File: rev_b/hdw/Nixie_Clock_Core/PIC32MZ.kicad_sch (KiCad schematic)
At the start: 3 parts

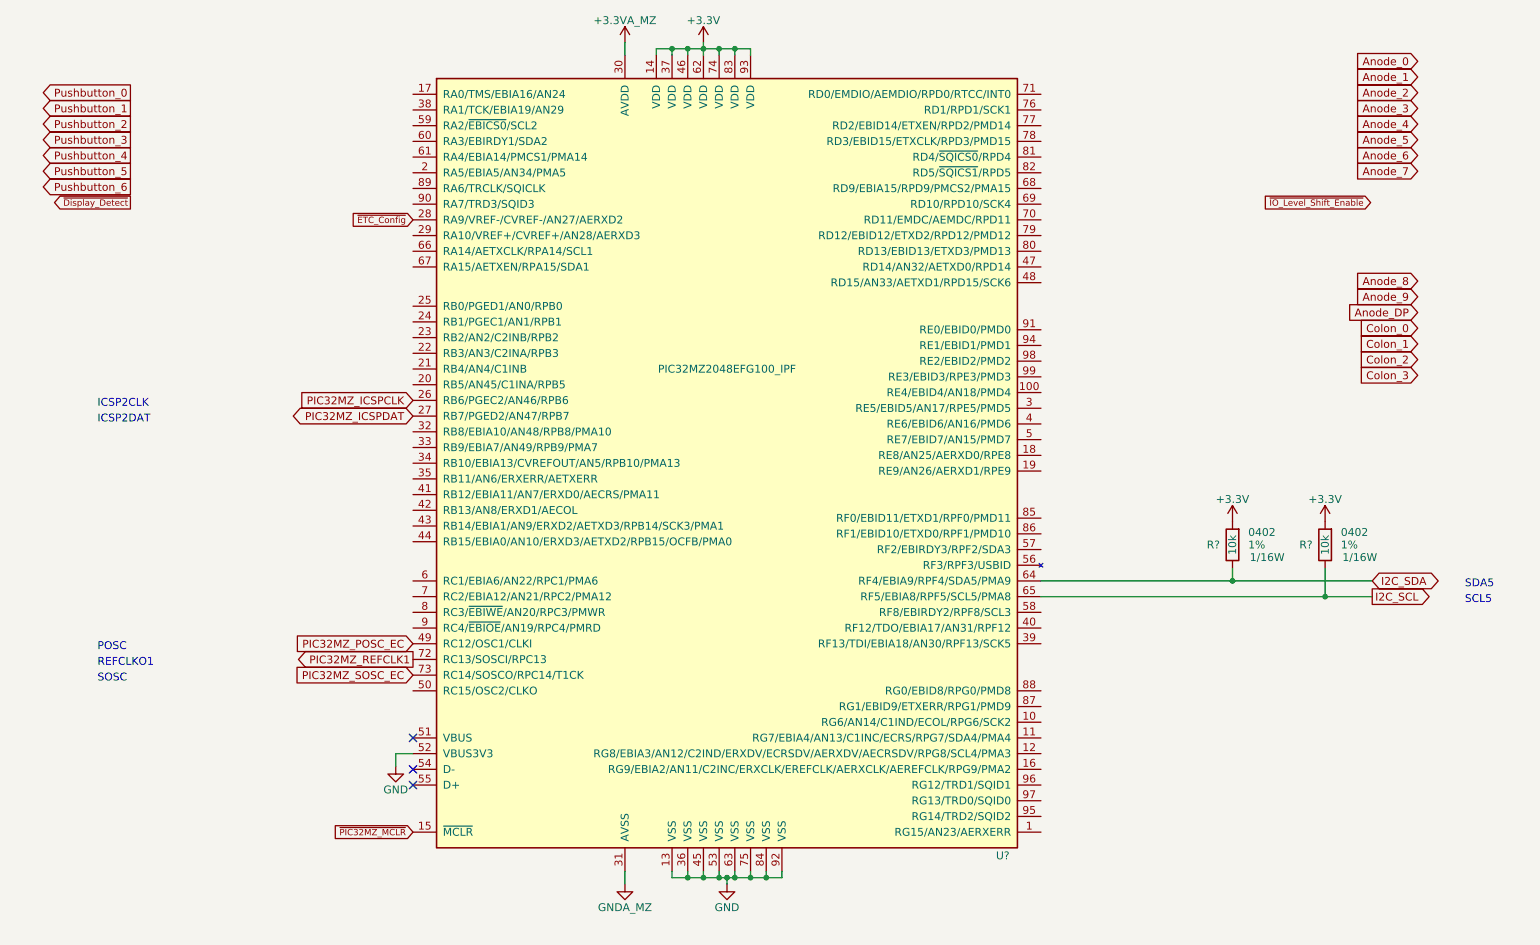
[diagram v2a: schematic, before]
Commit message: more schematic progress, assigning signals to MCU"
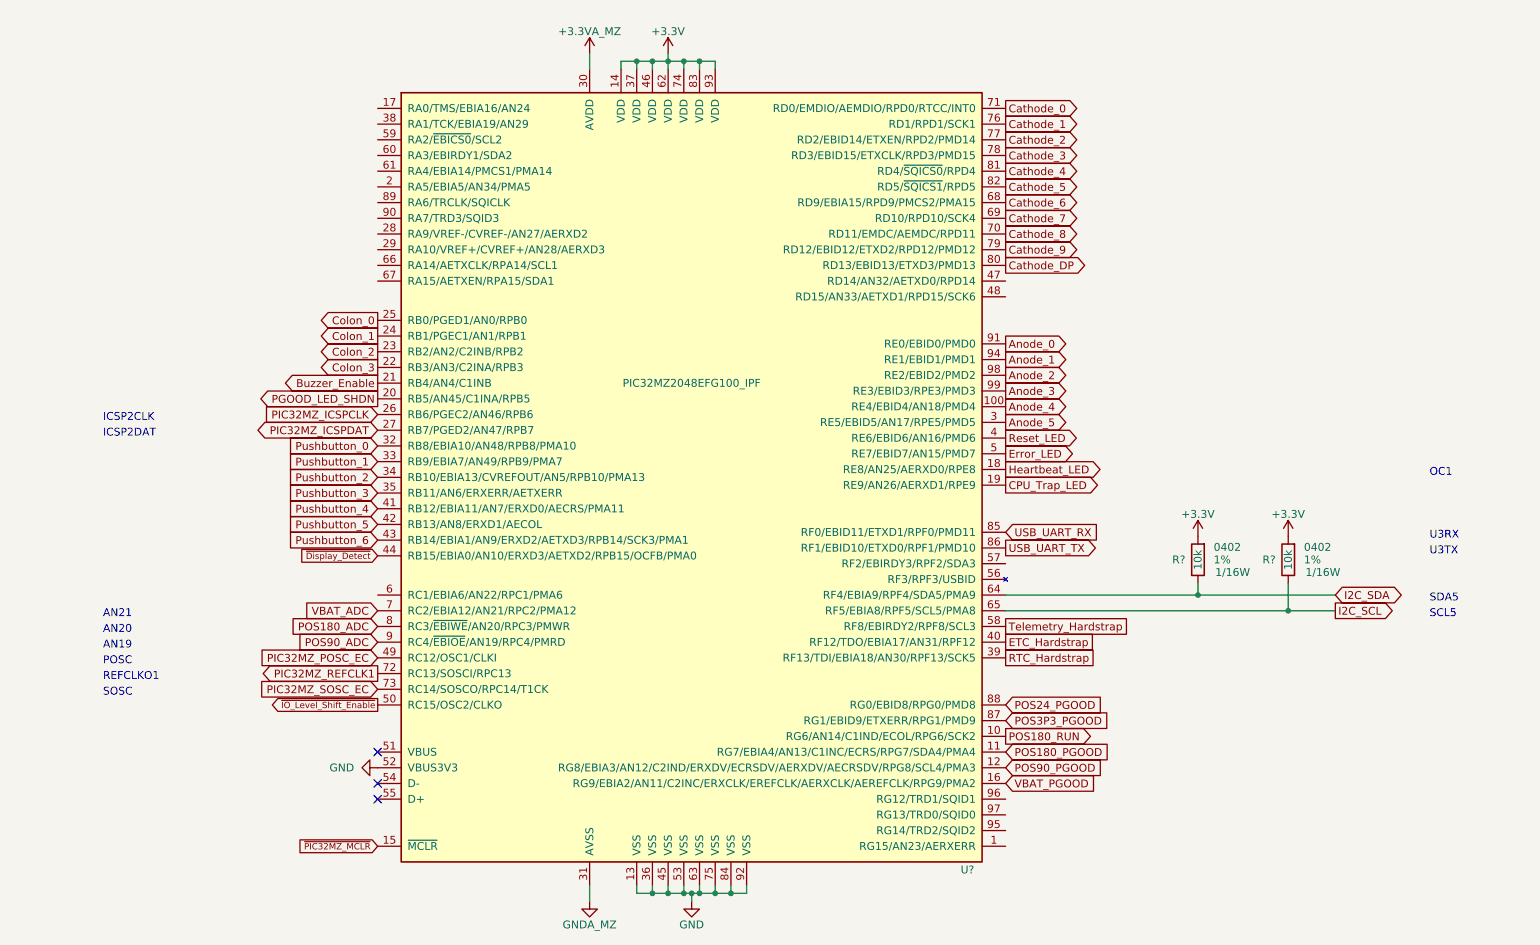
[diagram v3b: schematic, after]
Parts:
- removed U?: PIC32MZ2048EFG100_IPF, Housings_QFP:TQFP-100_14x14mm_Pitch0.5mm, symbol Custom_Library:PIC32MZ2048EFG100_IPF
- added U?: PIC32MZ2048EFG100_IPF, Housings_QFP:TQFP-100_14x14mm_Pitch0.5mm, symbol Custom Library:PIC32MZ2048EFG100_IPF
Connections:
- net +3.3V: now also U?.14 (VDD), U?.37 (VDD), U?.46 (VDD), U?.62 (VDD), U?.74 (VDD), U?.83 (VDD), U?.93 (VDD)
- net +3.3VA_MZ: now also U?.30 (AVDD)
- net Anode_0: now also U?.91 (RE0/EBID0/PMD0)
- net Anode_1: now also U?.94 (RE1/EBID1/PMD1)
- net Anode_2: now also U?.98 (RE2/EBID2/PMD2)
- net Anode_3: now also U?.99 (RE3/EBID3/RPE3/PMD3)
- net Anode_4: now also U?.100 (RE4/EBID4/AN18/PMD4)
- net Anode_5: now also U?.3 (RE5/EBID5/AN17/RPE5/PMD5)
- net Colon_0: now also U?.25 (RB0/PGED1/AN0/RPB0)
- net Colon_1: now also U?.24 (RB1/PGEC1/AN1/RPB1)
- net Colon_2: now also U?.23 (RB2/AN2/C2INB/RPB2)
- net Colon_3: now also U?.22 (RB3/AN3/C2INA/RPB3)
- net GND: now also U?.13 (VSS), U?.36 (VSS), U?.45 (VSS), U?.52 (VBUS3V3), U?.53 (VSS), U?.63 (VSS), U?.75 (VSS), U?.84 (VSS), U?.92 (VSS)
- net GNDA_MZ: now also U?.31 (AVSS)
- net I2C_SCL: now also U?.65 (RF5/EBIA8/RPF5/SCL5/PMA8)
- net I2C_SDA: now also U?.64 (RF4/EBIA9/RPF4/SDA5/PMA9)
- net PIC32MZ_ICSPCLK: now also U?.26 (RB6/PGEC2/AN46/RPB6)
- net PIC32MZ_ICSPDAT: now also U?.27 (RB7/PGED2/AN47/RPB7)
- net PIC32MZ_POSC_EC: now also U?.49 (RC12/OSC1/CLKI)
- net PIC32MZ_REFCLK1: now also U?.72 (RC13/SOSCI/RPC13)
- net PIC32MZ_SOSC_EC: now also U?.73 (RC14/SOSCO/RPC14/T1CK)
- net Pushbutton_0: now also U?.32 (RB8/EBIA10/AN48/RPB8/PMA10)
- net Pushbutton_1: now also U?.33 (RB9/EBIA7/AN49/RPB9/PMA7)
- net Pushbutton_2: now also U?.34 (RB10/EBIA13/CVREFOUT/AN5/RPB10/PMA13)
- net Pushbutton_3: now also U?.35 (RB11/AN6/ERXERR/AETXERR)
- net Pushbutton_4: now also U?.41 (RB12/EBIA11/AN7/ERXD0/AECRS/PMA11)
- net Pushbutton_5: now also U?.42 (RB13/AN8/ERXD1/AECOL)
- net Pushbutton_6: now also U?.43 (RB14/EBIA1/AN9/ERXD2/AETXD3/RPB14/SCK3/PMA1)
- net ~{Display_Detect}: now also U?.44 (RB15/EBIA0/AN10/ERXD3/AETXD2/RPB15/OCFB/PMA0)
- net ~{IO_Level_Shift_Enable}: now also U?.50 (RC15/OSC2/CLKO)
- net ~{PIC32MZ_MCLR}: now also U?.15 (~{MCLR})
- new net Buzzer_Enable: U?.21 (RB4/AN4/C1INB)
- new net CPU_Trap_LED: U?.19 (RE9/AN26/AERXD1/RPE9)
- new net Cathode_0: U?.71 (RD0/EMDIO/AEMDIO/RPD0/RTCC/INT0)
- new net Cathode_1: U?.76 (RD1/RPD1/SCK1)
- new net Cathode_2: U?.77 (RD2/EBID14/ETXEN/RPD2/PMD14)
- new net Cathode_3: U?.78 (RD3/EBID15/ETXCLK/RPD3/PMD15)
- new net Cathode_4: U?.81 (RD4/~{SQICS0}/RPD4)
- new net Cathode_5: U?.82 (RD5/~{SQICS1}/RPD5)
- new net Cathode_6: U?.68 (RD9/EBIA15/RPD9/PMCS2/PMA15)
- new net Cathode_7: U?.69 (RD10/RPD10/SCK4)
- new net Cathode_8: U?.70 (RD11/EMDC/AEMDC/RPD11)
- new net Cathode_9: U?.79 (RD12/EBID12/ETXD2/RPD12/PMD12)
- new net Cathode_DP: U?.80 (RD13/EBID13/ETXD3/PMD13)
- new net ETC_Hardstrap: U?.40 (RF12/TDO/EBIA17/AN31/RPF12)
- new net Error_LED: U?.5 (RE7/EBID7/AN15/PMD7)
- new net Heartbeat_LED: U?.18 (RE8/AN25/AERXD0/RPE8)
- new net PGOOD_LED_SHDN: U?.20 (RB5/AN45/C1INA/RPB5)
- new net POS180_ADC: U?.8 (RC3/~{EBIWE}/AN20/RPC3/PMWR)
- new net POS180_PGOOD: U?.11 (RG7/EBIA4/AN13/C1INC/ECRS/RPG7/SDA4/PMA4)
- new net POS180_RUN: U?.10 (RG6/AN14/C1IND/ECOL/RPG6/SCK2)
- new net POS24_PGOOD: U?.88 (RG0/EBID8/RPG0/PMD8)
- new net POS3P3_PGOOD: U?.87 (RG1/EBID9/ETXERR/RPG1/PMD9)
- new net POS90_ADC: U?.9 (RC4/~{EBIOE}/AN19/RPC4/PMRD)
- new net POS90_PGOOD: U?.12 (RG8/EBIA3/AN12/C2IND/ERXDV/ECRSDV/AERXDV/AECRSDV/RPG8/SCL4/PMA3)
- new net RTC_Hardstrap: U?.39 (RF13/TDI/EBIA18/AN30/RPF13/SCK5)
- new net Reset_LED: U?.4 (RE6/EBID6/AN16/PMD6)
- new net Telemetry_Hardstrap: U?.58 (RF8/EBIRDY2/RPF8/SCL3)
- new net USB_UART_RX: U?.85 (RF0/EBID11/ETXD1/RPF0/PMD11)
- new net USB_UART_TX: U?.86 (RF1/EBID10/ETXD0/RPF1/PMD10)
- new net VBAT_ADC: U?.7 (RC2/EBIA12/AN21/RPC2/PMA12)
- new net VBAT_PGOOD: U?.16 (RG9/EBIA2/AN11/C2INC/ERXCLK/EREFCLK/AERXCLK/AEREFCLK/RPG9/PMA2)
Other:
- note added: "AN19"
- note added: "AN20"
- note added: "AN21"
- note added: "OC1"
- note added: "U3RX"
- note added: "U3TX"
- moved on the sheet: R?

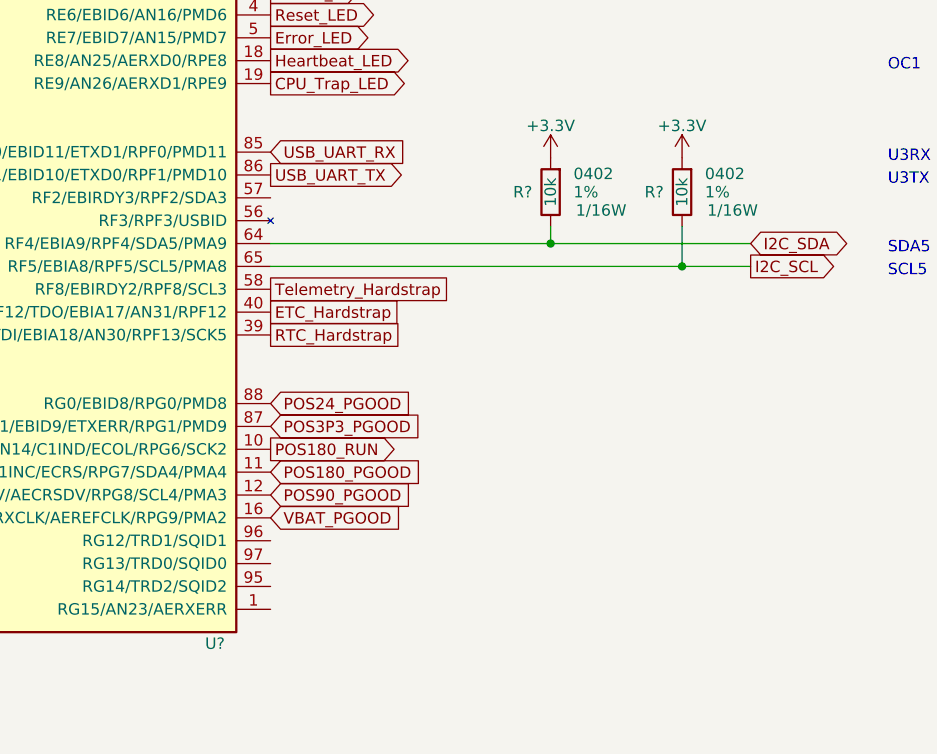
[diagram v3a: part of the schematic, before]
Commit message: updated footprints, ran some DRC
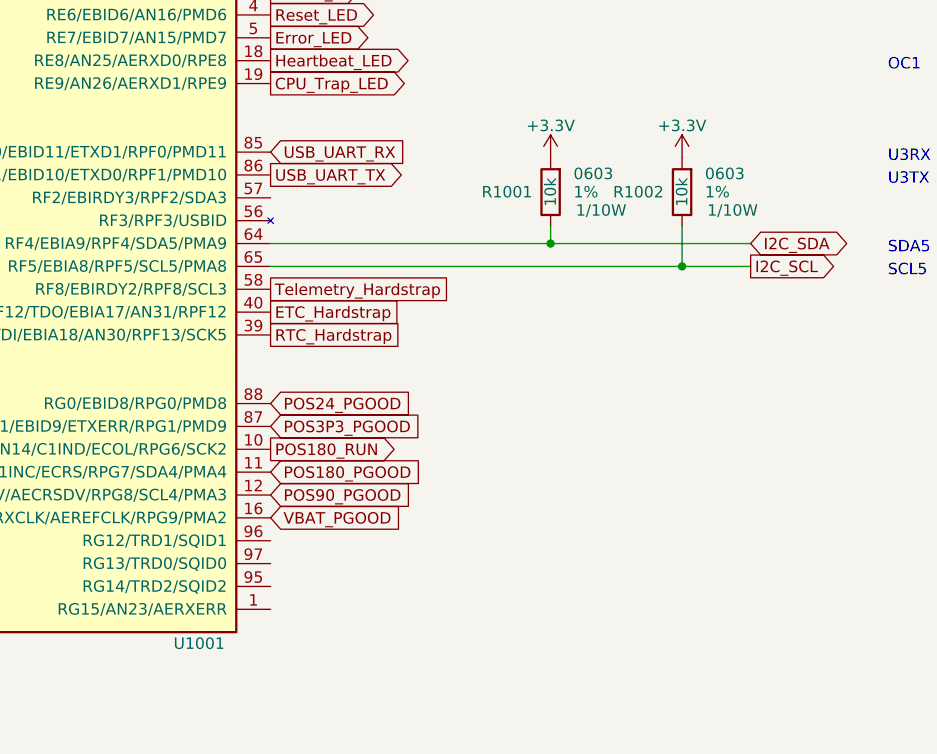
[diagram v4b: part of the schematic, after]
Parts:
- R1001, R1002: renamed from R?; footprint Resistors_SMD:R_0402 -> Resistors_SMD:R_0603; Digi-Key PN RMCF0402FT10K0CT-ND -> (none); Wattage 1/16W -> 1/10W; display_footprint 0402 -> 0603
- gave numbers to parts that had none: 1
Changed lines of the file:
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@@
   (symbol (lib_id "Custom_Library:R_Custom") (at 205.74 106.045 0) (unit 1)
     (in_bom yes) (on_board yes) (dnp no)
-    (property "Reference" "R?" (at 203.708 106.045 0)
+    (property "Reference" "R1001" (at 203.708 106.045 0)
       (effects (font (size 1.27 1.27)) (justify right))
     )
@@
       (effects (font (size 1.27 1.27)))
     )
-    (property "Footprint" "Resistors_SMD:R_0402" (at 205.74 106.045 0)
+    (property "Footprint" "Resistors_SMD:R_0603" (at 205.74 106.045 0)
       (effects (font (size 1.27 1.27)) hide)
     )
@@
       (effects (font (size 1.27 1.27)) hide)
     )
-    (property "display_footprint" "0402" (at 208.28 104.013 0)
+    (property "display_footprint" "0603" (at 208.28 104.013 0)
       (effects (font (size 1.27 1.27)) (justify left))
     )
@@
       (effects (font (size 1.27 1.27)) (justify left))
     )
-    (property "Wattage" "1/16W" (at 208.534 108.077 0)
-      (effects (font (size 1.27 1.27)) (justify left))
-    )
-    (property "Digi-Key PN" "RMCF0402FT10K0CT-ND" (at 205.74 106.045 0)
+    (property "Wattage" "1/10W" (at 208.534 108.077 0)
+      (effects (font (size 1.27 1.27)) (justify left))
+    )
+    (property "Digi-Key PN" "" (at 205.74 106.045 0)
       (effects (font (size 1.27 1.27)) hide)
     )
@@
       (project "Nixie_Clock_Core"
         (path "/16fdce21-b570-4d81-a458-e8839d611806/f7cc5c4d-c1a6-4096-b212-cb6ae1584770"
-          (reference "R?") (unit 1)
+          (reference "R1001") (unit 1)
         )
       )
@@
   (symbol (lib_id "Custom_Library:+3.3VA_MZ") (at 107.315 24.13 0) (unit 1)
     (in_bom yes) (on_board yes) (dnp no)
-    (property "Reference" "#PWR?" (at 107.315 27.94 0)
+    (property "Reference" "#PWR01002" (at 107.315 27.94 0)
       (effects (font (size 1.27 1.27)) hide)
     )
@@
       (project "Nixie_Clock_Core"
         (path "/16fdce21-b570-4d81-a458-e8839d611806/f7cc5c4d-c1a6-4096-b212-cb6ae1584770"
-          (reference "#PWR?") (unit 1)
+          (reference "#PWR01002") (unit 1)
         )
       )
@@
   (symbol (lib_id "Custom_Library:R_Custom") (at 220.345 106.045 0) (unit 1)
     (in_bom yes) (on_board yes) (dnp no)
-    (property "Reference" "R?" (at 218.313 106.045 0)
+    (property "Reference" "R1002" (at 218.313 106.045 0)
       (effects (font (size 1.27 1.27)) (justify right))
     )
@@
       (effects (font (size 1.27 1.27)))
     )
-    (property "Footprint" "Resistors_SMD:R_0402" (at 220.345 106.045 0)
+    (property "Footprint" "Resistors_SMD:R_0603" (at 220.345 106.045 0)
       (effects (font (size 1.27 1.27)) hide)
     )
@@
       (effects (font (size 1.27 1.27)) hide)
     )
-    (property "display_footprint" "0402" (at 222.885 104.013 0)
+    (property "display_footprint" "0603" (at 222.885 104.013 0)
       (effects (font (size 1.27 1.27)) (justify left))
     )
@@
       (effects (font (size 1.27 1.27)) (justify left))
     )
-    (property "Wattage" "1/16W" (at 223.139 108.077 0)
-      (effects (font (size 1.27 1.27)) (justify left))
-    )
-    (property "Digi-Key PN" "RMCF0402FT10K0CT-ND" (at 220.345 106.045 0)
+    (property "Wattage" "1/10W" (at 223.139 108.077 0)
+      (effects (font (size 1.27 1.27)) (justify left))
+    )
+    (property "Digi-Key PN" "" (at 220.345 106.045 0)
       (effects (font (size 1.27 1.27)) hide)
     )
@@
       (project "Nixie_Clock_Core"
         (path "/16fdce21-b570-4d81-a458-e8839d611806/f7cc5c4d-c1a6-4096-b212-cb6ae1584770"
-          (reference "R?") (unit 1)
+          (reference "R1002") (unit 1)
         )
       )
@@
   (symbol (lib_id "power:+3.3V") (at 120.015 24.13 0) (unit 1)
     (in_bom yes) (on_board yes) (dnp no)
-    (property "Reference" "#PWR?" (at 120.015 27.94 0)
+    (property "Reference" "#PWR01004" (at 120.015 27.94 0)
       (effects (font (size 1.27 1.27)) hide)
     )
@@
       (project "Nixie_Clock_Core"
         (path "/16fdce21-b570-4d81-a458-e8839d611806/f7cc5c4d-c1a6-4096-b212-cb6ae1584770"
-          (reference "#PWR?") (unit 1)
+          (reference "#PWR01004") (unit 1)
         )
       )
@@
   (symbol (lib_id "power:+3.3V") (at 220.345 102.235 0) (unit 1)
     (in_bom yes) (on_board yes) (dnp no)
-    (property "Reference" "#PWR?" (at 220.345 106.045 0)
+    (property "Reference" "#PWR01007" (at 220.345 106.045 0)
       (effects (font (size 1.27 1.27)) hide)
     )
@@
       (project "Nixie_Clock_Core"
         (path "/16fdce21-b570-4d81-a458-e8839d611806/f7cc5c4d-c1a6-4096-b212-cb6ae1584770"
-          (reference "#PWR?") (unit 1)
+          (reference "#PWR01007") (unit 1)
         )
       )
@@
   (symbol (lib_id "power:+3.3V") (at 205.74 102.235 0) (unit 1)
     (in_bom yes) (on_board yes) (dnp no)
-    (property "Reference" "#PWR?" (at 205.74 106.045 0)
+    (property "Reference" "#PWR01006" (at 205.74 106.045 0)
       (effects (font (size 1.27 1.27)) hide)
     )
@@
       (project "Nixie_Clock_Core"
         (path "/16fdce21-b570-4d81-a458-e8839d611806/f7cc5c4d-c1a6-4096-b212-cb6ae1584770"
-          (reference "#PWR?") (unit 1)
+          (reference "#PWR01006") (unit 1)
         )
       )
@@
   (symbol (lib_id "Custom_Library:GNDA_MZ") (at 107.315 161.29 0) (unit 1)
     (in_bom yes) (on_board yes) (dnp no)
-    (property "Reference" "#PWR?" (at 107.315 167.64 0)
+    (property "Reference" "#PWR01003" (at 107.315 167.64 0)
       (effects (font (size 1.27 1.27)) hide)
     )
@@
       (project "Nixie_Clock_Core"
         (path "/16fdce21-b570-4d81-a458-e8839d611806/f7cc5c4d-c1a6-4096-b212-cb6ae1584770"
-          (reference "#PWR?") (unit 1)
+          (reference "#PWR01003") (unit 1)
         )
       )
@@
   (symbol (lib_id "Custom Library:PIC32MZ2048EFG100_IPF") (at 123.825 92.71 0) (unit 1)
     (in_bom yes) (on_board yes) (dnp no)
-    (property "Reference" "U?" (at 169.545 156.21 0)
+    (property "Reference" "U1001" (at 169.545 156.21 0)
       (effects (font (size 1.27 1.27)) (justify right))
     )
@@
       (project "Nixie_Clock_Core"
         (path "/16fdce21-b570-4d81-a458-e8839d611806/f7cc5c4d-c1a6-4096-b212-cb6ae1584770"
-          (reference "U?") (unit 1)
+          (reference "U1001") (unit 1)
         )
       )
@@
   (symbol (lib_id "power:GND") (at 123.825 161.29 0) (unit 1)
     (in_bom yes) (on_board yes) (dnp no)
-    (property "Reference" "#PWR?" (at 123.825 167.64 0)
+    (property "Reference" "#PWR01005" (at 123.825 167.64 0)
       (effects (font (size 1.27 1.27)) hide)
     )
@@
       (project "Nixie_Clock_Core"
         (path "/16fdce21-b570-4d81-a458-e8839d611806/f7cc5c4d-c1a6-4096-b212-cb6ae1584770"
-          (reference "#PWR?") (unit 1)
-        )
-      )
+          (reference "#PWR01005") (unit 1)
+        )
+      )
